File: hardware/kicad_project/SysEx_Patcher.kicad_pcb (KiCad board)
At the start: 4 copper layers, 172 x 228 mm, 87 parts, among them J1 MIDI_IN, J10 JACK6.35, J2 MIDI_OUT, J3 DC_5V, J4 BAT_PWR, J5 OLED, SW1 prog/MIDI, SW2 SW, SW3 SW, SW4 SW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

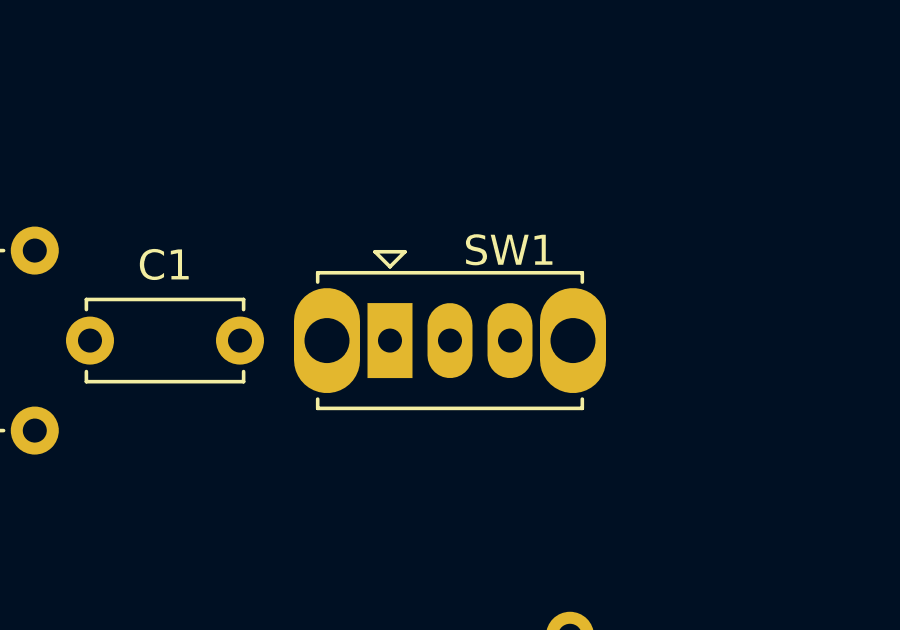
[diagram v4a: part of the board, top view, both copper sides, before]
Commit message: hardware: remove SW1 prog/MIDI switch, wire 6N138 -> RX0 directly
The 6N138 output (open-collector + 10k pull-up R5) is now hardwired to RX0 (D0)
instead of through the SPDT prog/MIDI switch. MIDI IN works permanently; only
caveat is not flashing firmware while MIDI is actively streaming in. Reroute:
0 unconnected, DRC clean; schematic + fab Gerbers + docs updated.
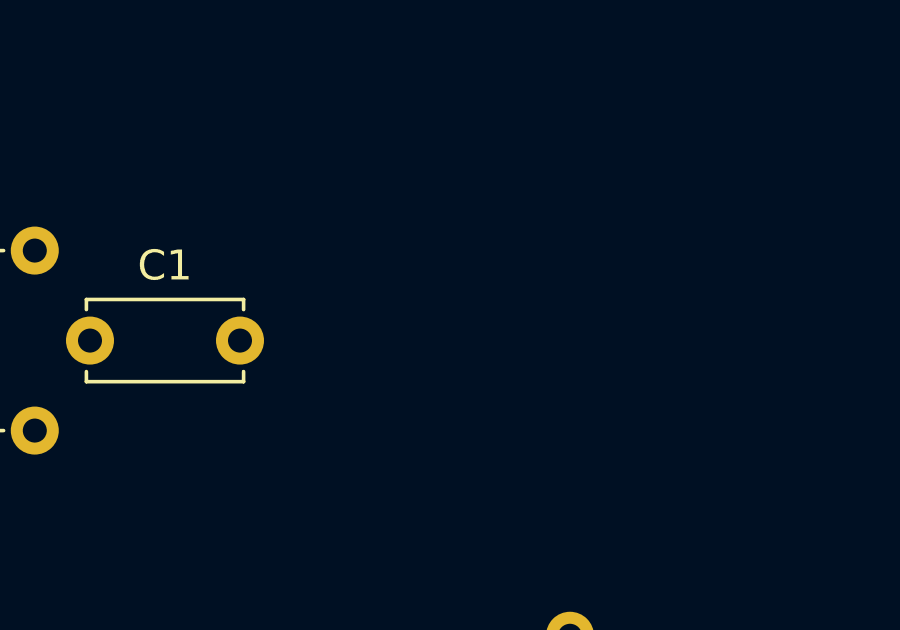
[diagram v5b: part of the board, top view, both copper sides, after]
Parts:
- removed SW1: prog/MIDI, Button_Switch_THT:SW_Slide_SPDT_Straight_CK_OS102011MS2Q
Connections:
- R5 pad 1: OPTO_VO -> D0_RX
- U1 pad 6: OPTO_VO -> D0_RX

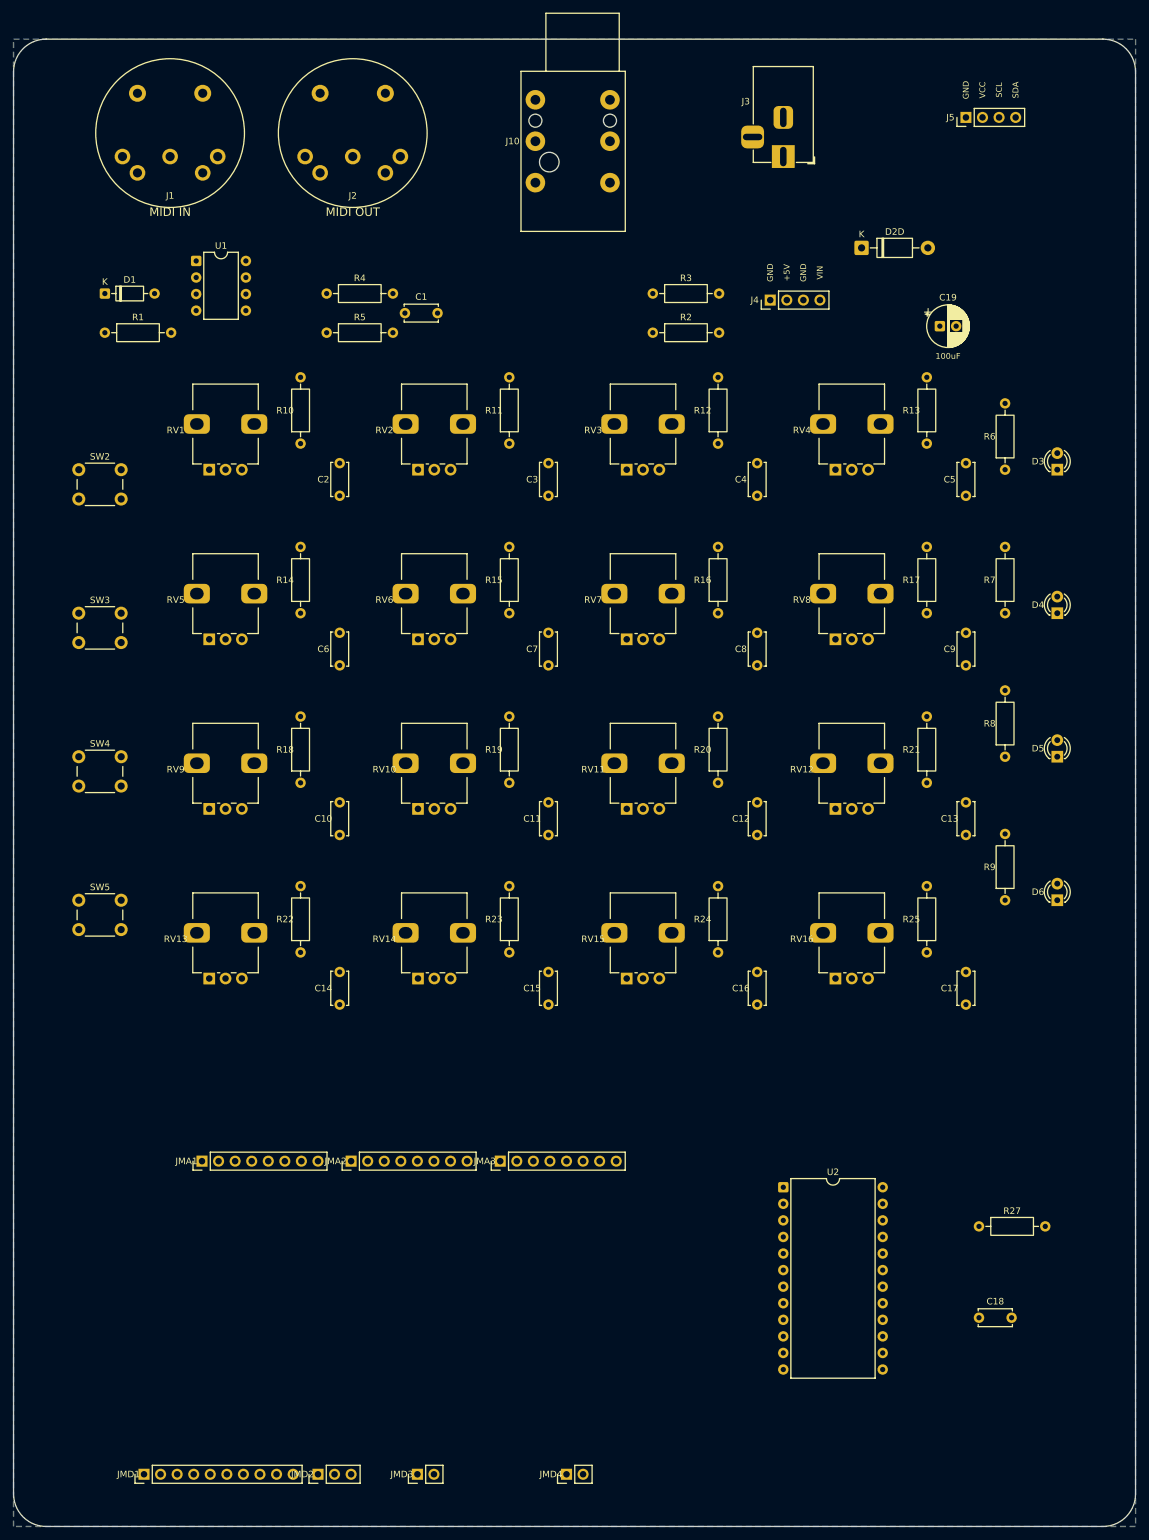
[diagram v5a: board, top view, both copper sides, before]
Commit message: hardware: compact shield — Mega now sits UNDER the pots (like the original)
- pot row pitch 24mm so the two Mega header rows tuck into the gaps between pot
  rows (analog y72, digital y120); the Mega plugs underneath the pot grid
- board shrinks 172x228 -> 172x172
- mux 4067 + jack filter relocated below the pot grid (clear of the Mega)
- MIDI-out resistors R2/R3 moved to clear the raised pot-filter column
- footprint courtyards stripped (stacked board: components legitimately sit over
  the Mega headers, so courtyard overlaps are false positives)
- reroute 0 unconnected, DRC clean; fab Gerbers + previews + doc updated
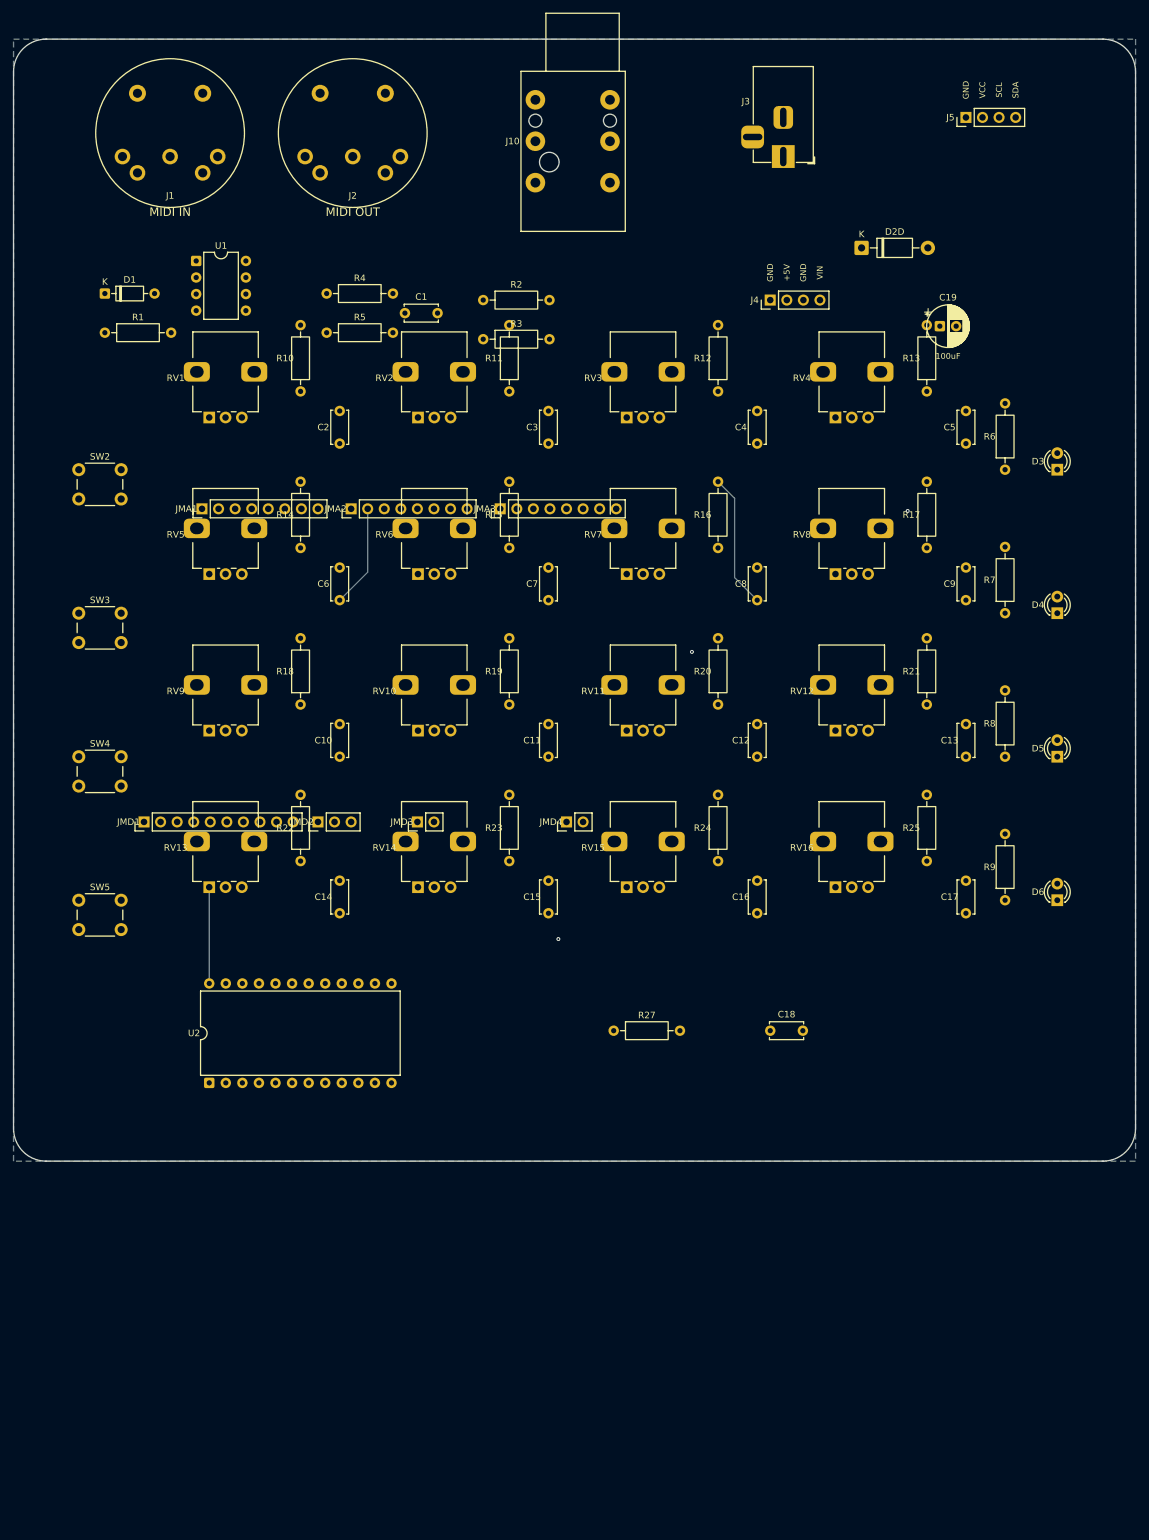
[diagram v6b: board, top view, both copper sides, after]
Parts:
- moved JMA1 100.0 mm to (48.9, 92.0)
- moved JMA2 100.0 mm to (71.8, 92.0)
- moved JMA3 100.0 mm to (94.6, 92.0)
- moved JMD1 100.0 mm to (40.0, 140.0)
- moved JMD2 100.0 mm to (66.7, 140.0)
- moved JMD3 100.0 mm to (81.9, 140.0)
- moved JMD4 100.0 mm to (104.8, 140.0)
- moved U2 89.4 mm to (50.0, 180.0), turned to 90 degrees
- moved R27 63.5 mm to (112.0, 172.0)
- moved C18 54.4 mm to (136.0, 172.0)
- moved R3 26.9 mm to (92.0, 66.0)
- moved R2 26.5 mm to (92.0, 60.0)
- moved C14 14.0 mm to (70.0, 154.0)
- moved C15 14.0 mm to (102.0, 154.0)
- moved C16 14.0 mm to (134.0, 154.0)
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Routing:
- net +5V: track 0.00 -> 606.8 mm
- net D20_SDA: track 0.00 -> 139.9 mm
- net A15: track 0.00 -> 135.7 mm, vias 0 -> 1
- net JACK_W: track 0.00 -> 135.7 mm
- net D21_SCL: track 0.00 -> 134.4 mm
- net VIN_RAW: track 0.00 -> 133.4 mm
- net MUX_CH0: track 0.00 -> 127.1 mm
- net D12: track 0.00 -> 123.5 mm
- net D11: track 0.00 -> 117.0 mm
- net D9: track 0.00 -> 114.1 mm
- net D10: track 0.00 -> 111.0 mm
- net D0_RX: track 0.00 -> 103.5 mm
- net A14: track 0.00 -> 89.7 mm, vias 0 -> 1
- net A12: track 0.00 -> 86.0 mm
- net D1_TX: track 0.00 -> 82.4 mm
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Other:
- board size 172 x 228 mm -> 172 x 172 mm

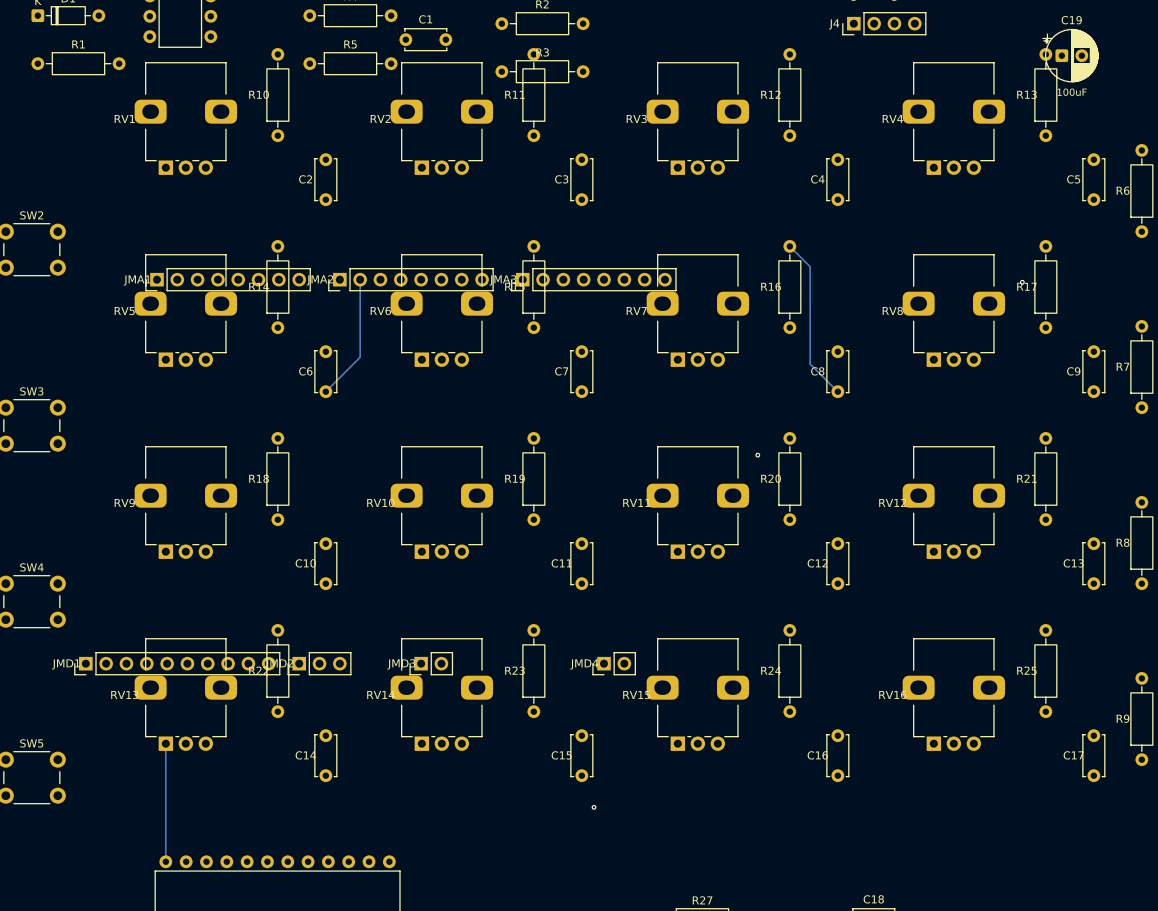
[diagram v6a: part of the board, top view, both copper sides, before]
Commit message: hardware: fix Mega-under-pots layout — header rows now clear of pot bodies
The pot footprint body extends ~13mm above its origin (not the 7mm pin span),
so the header rows were landing under the pot bodies. Fixes:
- RC filters made horizontal (beside the pot) so each row is shorter
- header rows recentred in the real gaps between pot BODIES (analog y66, digital y114)
- routing clearance bumped to 0.25mm to clear a track/mounting-pad near-miss
Reroute: 0 unconnected, DRC clean. Board 172x172, Mega plugs under the pot grid.
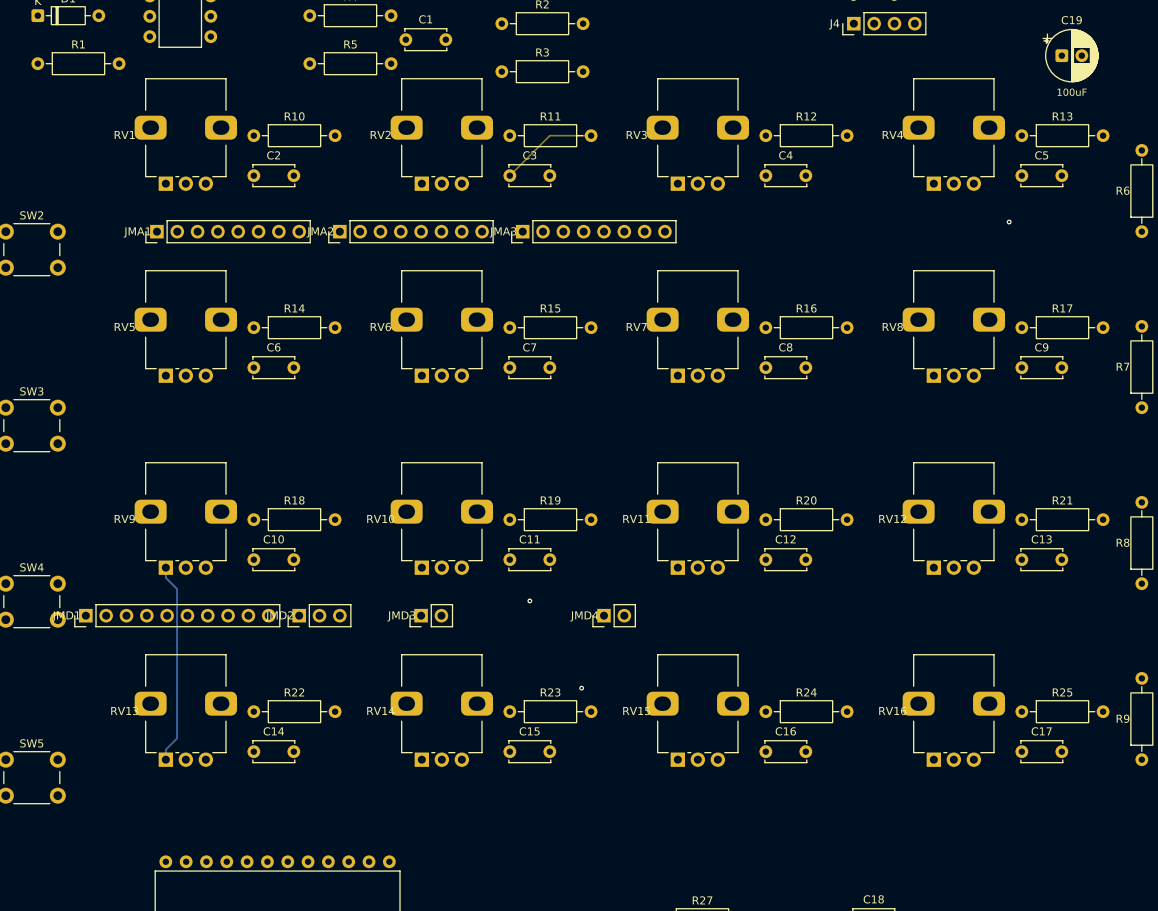
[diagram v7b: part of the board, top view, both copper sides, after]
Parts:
- moved C10 9.49 mm to (61.0, 127.0), turned to 0 degrees
- moved C11 9.49 mm to (93.0, 127.0), turned to 0 degrees
- moved C12 9.49 mm to (125.0, 127.0), turned to 0 degrees
- moved C13 9.49 mm to (157.0, 127.0), turned to 0 degrees
- moved C14 9.49 mm to (61.0, 151.0), turned to 0 degrees
- moved C15 9.49 mm to (93.0, 151.0), turned to 0 degrees
- moved C16 9.49 mm to (125.0, 151.0), turned to 0 degrees
- moved C17 9.49 mm to (157.0, 151.0), turned to 0 degrees
- moved C2 9.49 mm to (61.0, 79.0), turned to 0 degrees
- moved C3 9.49 mm to (93.0, 79.0), turned to 0 degrees
- moved C4 9.49 mm to (125.0, 79.0), turned to 0 degrees
- moved C5 9.49 mm to (157.0, 79.0), turned to 0 degrees
- moved C6 9.49 mm to (61.0, 103.0), turned to 0 degrees
- moved C7 9.49 mm to (93.0, 103.0), turned to 0 degrees
- moved C8 9.49 mm to (125.0, 103.0), turned to 0 degrees
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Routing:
- net +5V: track 606.8 -> 640.4 mm
- net A5: track 46.7 -> 23.7 mm
- net A11: track 75.7 -> 97.7 mm
- net A12: track 86.0 -> 67.4 mm
- net A8: track 64.3 -> 45.7 mm
- net MUX_CH0: track 127.1 -> 110.9 mm
- net A6: track 47.7 -> 60.2 mm
- net A7: track 67.2 -> 78.7 mm
- net A14: track 89.7 -> 101.2 mm
- net D0_RX: track 103.5 -> 95.7 mm
- net D13: track 38.0 -> 45.8 mm
- net JACK_W: track 135.7 -> 143.3 mm
- net D7: track 70.4 -> 63.3 mm
- net A0: track 31.4 -> 24.5 mm
- net A10: track 59.4 -> 65.8 mm
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
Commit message: hardware: shift button column left to clear Mega digital header pins
SW2-SW5 moved from x=10 to x=6 (board x30->x26) so SW4 no longer crowds
the JMD1 digital header row. Re-routed (0 unconnected), DRC clean of
electrical violations, gerbers/drill/previews regenerated.
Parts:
- moved SW2 4.00 mm to (26.0, 86.0)
- moved SW3 4.00 mm to (26.0, 108.0)
- moved SW4 4.00 mm to (26.0, 130.0)
- moved SW5 4.00 mm to (26.0, 152.0)
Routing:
- net D6: track 26.9 -> 30.9 mm
- net D5: track 31.2 -> 34.2 mm
- net D13: track 45.8 -> 42.9 mm
- net D4: track 44.7 -> 46.6 mm
- net +5V: track 640.4 -> 642.2 mm
- net D7: track 63.3 -> 65.0 mm
- net D8: track 47.1 -> 47.7 mm
